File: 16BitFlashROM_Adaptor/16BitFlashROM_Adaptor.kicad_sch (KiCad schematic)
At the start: 15 parts, among them J2 Right GPIO, J5 Right GPIO, U1 M29F160FT55N3E2

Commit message: - Updated Vic20 Flash Cart files to Ki-CAD 9.x - Cleaned up some component names and generated ibom's
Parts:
- J1: value ~ -> Address
- J2: value Right GPIO -> Right Pins
- J3: value ~ -> Reset
- J5: value Right GPIO -> Left Pins
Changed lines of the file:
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@@
 			)
 		)
-		(property "Value" "Right GPIO"
+		(property "Value" "Right Pins"
 			(at 273.291 94.1207 90)
 			(effects
@@
 			)
 		)
-		(property "Value" "Right GPIO"
+		(property "Value" "Left Pins"
 			(at 21.349 91.2993 90)
 			(effects
@@
 			)
 		)
-		(property "Value" "~"
+		(property "Value" "Address"
 			(at 106.8207 28.969 90)
 			(effects
@@
 			)
 		)
-		(property "Value" "~"
+		(property "Value" "Reset"
 			(at 81.1393 28.969 90)
 			(effects

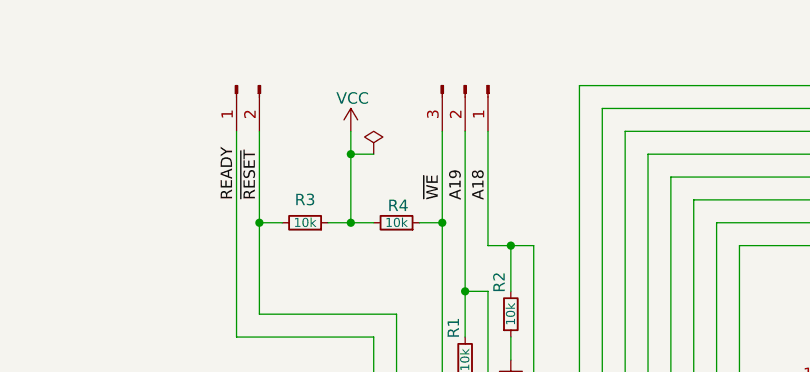
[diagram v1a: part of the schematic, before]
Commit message: - Added A Couple Of 5v Pins To Easily Jumper The Additional ROM Banks.
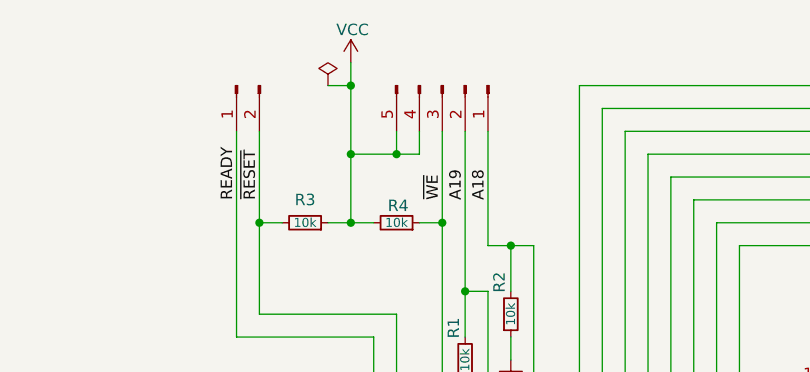
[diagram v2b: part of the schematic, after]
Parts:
- J1: footprint Connector_PinHeader_2.54mm:PinHeader_1x03_P2.54mm_Vertical -> Dave Footprints:PinHeader_Amiga_ROM; symbol Connector:Conn_01x03_Pin -> Connector:Conn_01x05_Pin
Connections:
- net VCC: now also J1.4 (Pin_4), J1.5 (Pin_5)
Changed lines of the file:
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@@
 	)
 	(junction
+		(at 99.06 38.1)
+		(diameter 0)
+		(color 0 0 0 0)
+	)
+	(junction
 		(at 106.68 53.34)
 		(diameter 0)
@@
 	)
 	(junction
+		(at 93.98 30.48)
+		(diameter 0)
+		(color 0 0 0 0)
+	)
+	(junction
 		(at 104.14 45.72)
 		(diameter 0)
@@
 	(wire
 		(pts
+			(xy 91.44 30.48) (xy 93.98 30.48)
+		)
+		(stroke
+			(width 0)
+			(type default)
+		)
+	)
+	(wire
+		(pts
 			(xy 93.98 45.72) (xy 96.52 45.72)
 		)
@@
 	(wire
 		(pts
-			(xy 60.96 137.16) (xy 185.42 137.16)
+			(xy 101.6 35.56) (xy 101.6 38.1)
 		)
 		(stroke
@@
 	(wire
 		(pts
-			(xy 208.28 91.44) (xy 208.28 116.84)
+			(xy 60.96 137.16) (xy 185.42 137.16)
 		)
 		(stroke
@@
 	(wire
 		(pts
-			(xy 104.14 88.9) (xy 142.24 88.9)
+			(xy 208.28 91.44) (xy 208.28 116.84)
 		)
 		(stroke
@@
 	(wire
 		(pts
-			(xy 220.98 78.74) (xy 220.98 104.14)
+			(xy 104.14 88.9) (xy 142.24 88.9)
 		)
 		(stroke
@@
 	(wire
 		(pts
-			(xy 175.26 93.98) (xy 205.74 93.98)
+			(xy 220.98 78.74) (xy 220.98 104.14)
 		)
 		(stroke
@@
 	(wire
 		(pts
-			(xy 127 38.1) (xy 248.92 38.1)
+			(xy 175.26 93.98) (xy 205.74 93.98)
 		)
 		(stroke
@@
 	(wire
 		(pts
-			(xy 93.98 35.56) (xy 93.98 38.1)
+			(xy 127 38.1) (xy 248.92 38.1)
 		)
 		(stroke
@@
 	(wire
 		(pts
+			(xy 99.06 38.1) (xy 101.6 38.1)
+		)
+		(stroke
+			(width 0)
+			(type default)
+		)
+	)
+	(wire
+		(pts
 			(xy 220.98 132.08) (xy 220.98 129.54)
 		)
@@
 	(wire
 		(pts
-			(xy 93.98 38.1) (xy 93.98 45.72)
+			(xy 93.98 27.94) (xy 93.98 30.48)
 		)
 		(stroke
@@
 	(wire
 		(pts
+			(xy 93.98 38.1) (xy 93.98 45.72)
+		)
+		(stroke
+			(width 0)
+			(type default)
+		)
+	)
+	(wire
+		(pts
 			(xy 254 71.12) (xy 266.7 71.12)
 		)
@@
 	(wire
 		(pts
+			(xy 99.06 35.56) (xy 99.06 38.1)
+		)
+		(stroke
+			(width 0)
+			(type default)
+		)
+	)
+	(wire
+		(pts
 			(xy 124.46 35.56) (xy 251.46 35.56)
 		)
@@
 	(wire
 		(pts
-			(xy 251.46 35.56) (xy 251.46 73.66)
+			(xy 93.98 30.48) (xy 93.98 38.1)
 		)
 		(stroke
@@
 	(wire
 		(pts
-			(xy 111.76 60.96) (xy 111.76 58.42)
+			(xy 251.46 35.56) (xy 251.46 73.66)
 		)
 		(stroke
@@
 	(wire
 		(pts
-			(xy 96.52 38.1) (xy 93.98 38.1)
+			(xy 111.76 60.96) (xy 111.76 58.42)
 		)
 		(stroke
@@
 	(wire
 		(pts
+			(xy 93.98 38.1) (xy 99.06 38.1)
+		)
+		(stroke
+			(width 0)
+			(type default)
+		)
+	)
+	(wire
+		(pts
 			(xy 187.96 111.76) (xy 175.26 111.76)
 		)
@@
 	)
 	(symbol
+		(lib_id "power:PWR_FLAG")
+		(at 91.44 30.48 0)
+		(unit 1)
+		(exclude_from_sim no)
+		(in_bom yes)
+		(on_board yes)
+		(dnp no)
+		(fields_autoplaced yes)
+		(property "Reference" "#FLG03"
+			(at 91.44 28.575 0)
+			(effects
+				(font
+					(size 1.27 1.27)
+				)
+				(hide yes)
+			)
+		)
+		(property "Value" "PWR_FLAG"
+			(at 91.44 25.4 0)
+			(effects
+				(font
+					(size 1.27 1.27)
+				)
+				(hide yes)
+			)
+		)
+		(property "Footprint" ""
+			(at 91.44 30.48 0)
+			(effects
+				(font
+					(size 1.27 1.27)
+				)
+				(hide yes)
+			)
+		)
+		(property "Datasheet" "~"
+			(at 91.44 30.48 0)
+			(effects
+				(font
+					(size 1.27 1.27)
+				)
+				(hide yes)
+			)
+		)
+		(property "Description" "Special symbol for telling ERC where power comes from"
+			(at 91.44 30.48 0)
+			(effects
+				(font
+					(size 1.27 1.27)
+				)
+				(hide yes)
+			)
+		)
+		(pin "1"
+		)
+		(instances
+			(project "16BitFlashROM_Adaptor"
+				(path "/26813dea-ac31-4359-98cd-29d1f4f9df4c"
+					(reference "#FLG03")
+					(unit 1)
+				)
+			)
+		)
+	)
+	(symbol
 		(lib_id "Connector:Conn_01x20_Pin")
 		(at 271.78 93.98 180)
@@
 	)
 	(symbol
-		(lib_id "power:PWR_FLAG")
-		(at 96.52 38.1 0)
-		(mirror y)
-		(unit 1)
-		(exclude_from_sim no)
-		(in_bom yes)
-		(on_board yes)
-		(dnp no)
-		(fields_autoplaced yes)
-		(property "Reference" "#FLG01"
-			(at 96.52 36.195 0)
-			(effects
-				(font
-					(size 1.27 1.27)
-				)
-				(hide yes)
-			)
-		)
-		(property "Value" "PWR_FLAG"
-			(at 96.52 33.02 0)
-			(effects
-				(font
-					(size 1.27 1.27)
-				)
-				(hide yes)
-			)
-		)
-		(property "Footprint" ""
-			(at 96.52 38.1 0)
-			(effects
-				(font
-					(size 1.27 1.27)
-				)
-				(hide yes)
-			)
-		)
-		(property "Datasheet" "~"
-			(at 96.52 38.1 0)
-			(effects
-				(font
-					(size 1.27 1.27)
-				)
-				(hide yes)
-			)
-		)
-		(property "Description" "Special symbol for telling ERC where power comes from"
-			(at 96.52 38.1 0)
-			(effects
-				(font
-					(size 1.27 1.27)
-				)
-				(hide yes)
-			)
-		)
-		(pin "1"
-		)
-		(instances
-			(project "16BitFlashROM_Adaptor"
-				(path "/26813dea-ac31-4359-98cd-29d1f4f9df4c"
-					(reference "#FLG01")
-					(unit 1)
-				)
-			)
-		)
-	)
-	(symbol
 		(lib_id "SamacSys_Parts:M29F160FT55N3E2")
 		(at 142.24 63.5 0)
@@
 	(symbol
 		(lib_id "power:VCC")
-		(at 93.98 35.56 0)
+		(at 93.98 27.94 0)
 		(mirror y)
 		(unit 1)
@@
 		(dnp no)
 		(property "Reference" "#PWR04"
-			(at 93.98 39.37 0)
+			(at 93.98 31.75 0)
 			(effects
 				(font
@@
 		)
 		(property "Value" "VCC"
-			(at 94.1767 31.9035 0)
+			(at 94.1767 24.2835 0)
 			(effects
 				(font
@@
 		)
 		(property "Footprint" ""
-			(at 93.98 35.56 0)
+			(at 93.98 27.94 0)
 			(effects
 				(font
@@
 		)
 		(property "Datasheet" ""
-			(at 93.98 35.56 0)
+			(at 93.98 27.94 0)
 			(effects
 				(font
@@
 		)
 		(property "Description" "Power symbol creates a global label with name \"VCC\""
-			(at 93.98 35.56 0)
+			(at 93.98 27.94 0)
 			(effects
 				(font
@@
 	)
 	(symbol
-		(lib_id "Connector:Conn_01x03_Pin")
-		(at 106.68 30.48 270)
+		(lib_id "Connector:Conn_01x05_Pin")
+		(at 104.14 30.48 270)
 		(unit 1)
 		(exclude_from_sim no)
@@
 		(dnp no)
 		(property "Reference" "J1"
-			(at 105.6937 27.8942 90)
+			(at 103.1537 27.8942 90)
 			(effects
 				(font
@@
 		)
 		(property "Value" "Address"
-			(at 106.8207 28.969 90)
+			(at 104.2807 28.969 90)
 			(effects
 				(font
@@
 			)
 		)
-		(property "Footprint" "Connector_PinHeader_2.54mm:PinHeader_1x03_P2.54mm_Vertical"
-			(at 106.68 30.48 0)
+		(property "Footprint" "Dave Footprints:PinHeader_Amiga_ROM"
+			(at 104.14 30.48 0)
 			(effects
 				(font
@@
 		)
 		(property "Datasheet" "~"
-			(at 106.68 30.48 0)
+			(at 104.14 30.48 0)
 			(effects
 				(font
@@
 			)
 		)
-		(property "Description" "Generic connector, single row, 01x03, script generated"
-			(at 106.68 30.48 0)
+		(property "Description" "Generic connector, single row, 01x05, script generated"
+			(at 104.14 30.48 0)
 			(effects
 				(font
@@
 		)
 		(property "Note" ""
-			(at 106.68 30.48 0)
+			(at 104.14 30.48 0)
 			(effects
 				(font
@@
 		)
 		(property "Voltage" ""
-			(at 106.68 30.48 0)
+			(at 104.14 30.48 0)
 			(effects
 				(font
@@
 		)
 		(property "class" ""
-			(at 106.68 30.48 0)
+			(at 104.14 30.48 0)
 			(effects
 				(font
@@
 		(pin "3"
 		)
+		(pin "4"
+		)
+		(pin "5"
+		)
 		(instances
